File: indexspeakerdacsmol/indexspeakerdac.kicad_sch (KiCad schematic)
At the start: 34 parts, among them IC1 MAX98360AEFB+T, IC2 MAX98360AEFB+T, IC3 W25Q16JVUXIQ_TR, J1 Conn_01x04_Pin, J2 Conn_01x04_Pin, U1 RP2040, U2 MIC5317-3.3xM5, Y1 Crystal_GND24

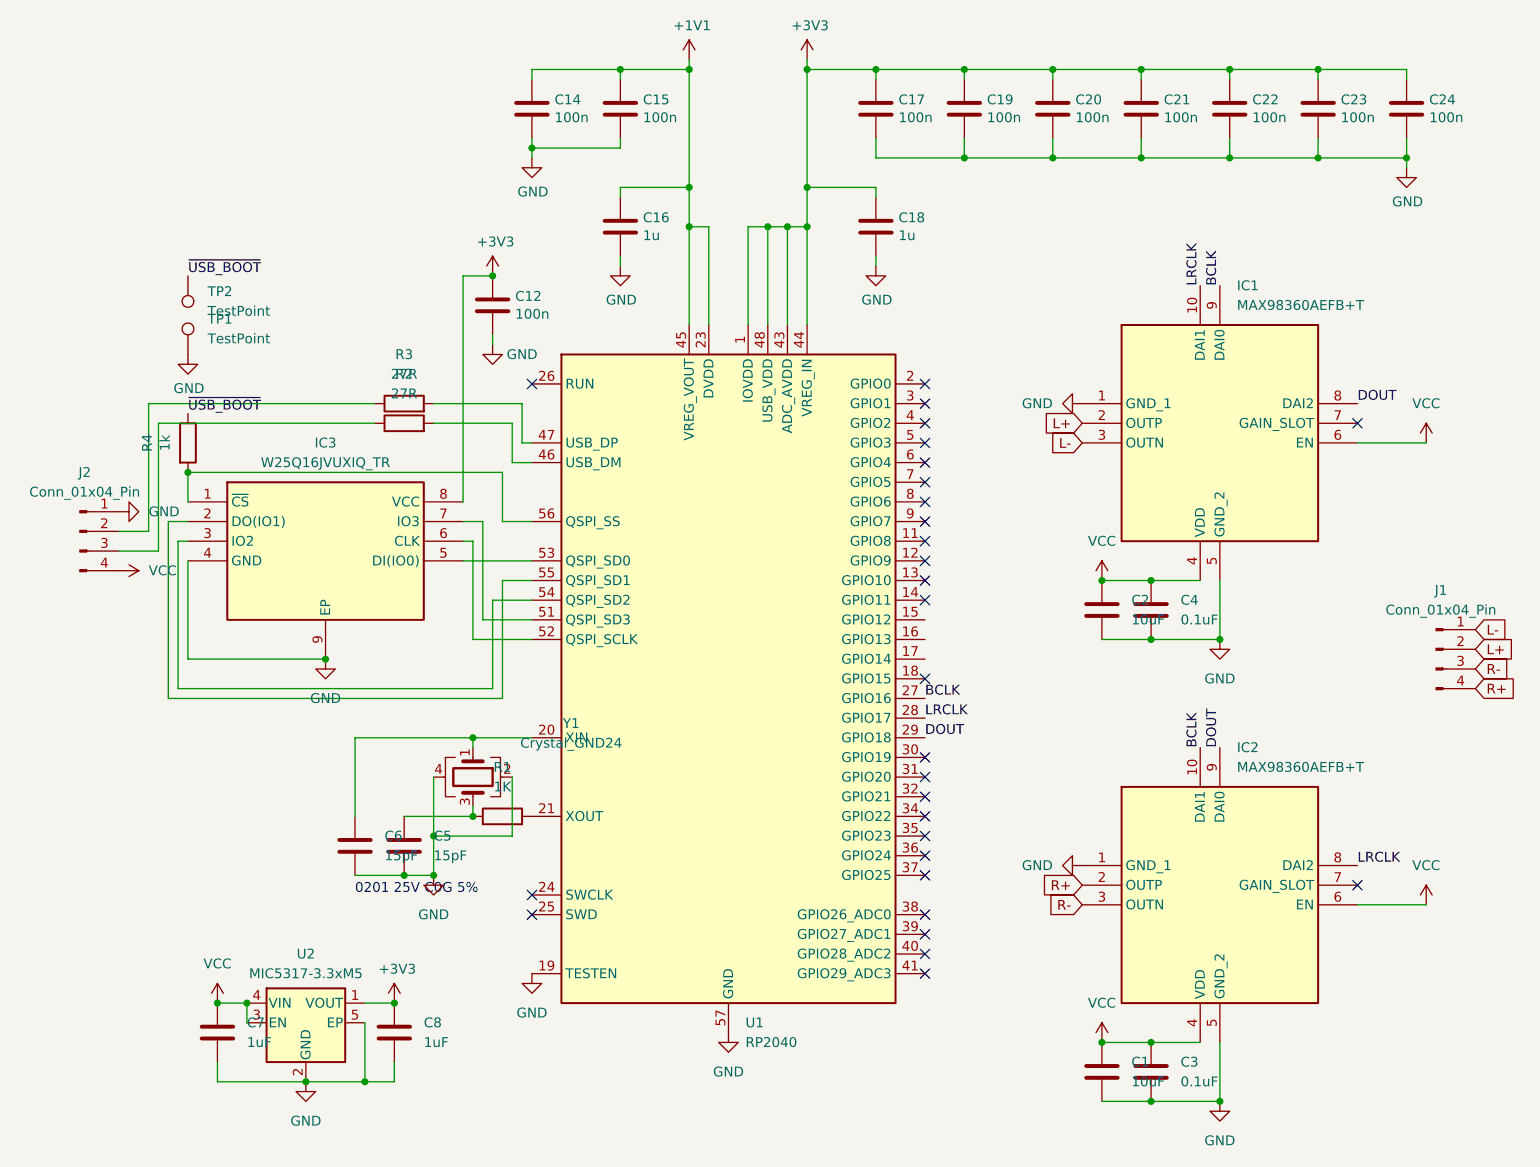
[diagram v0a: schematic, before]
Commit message: add bom
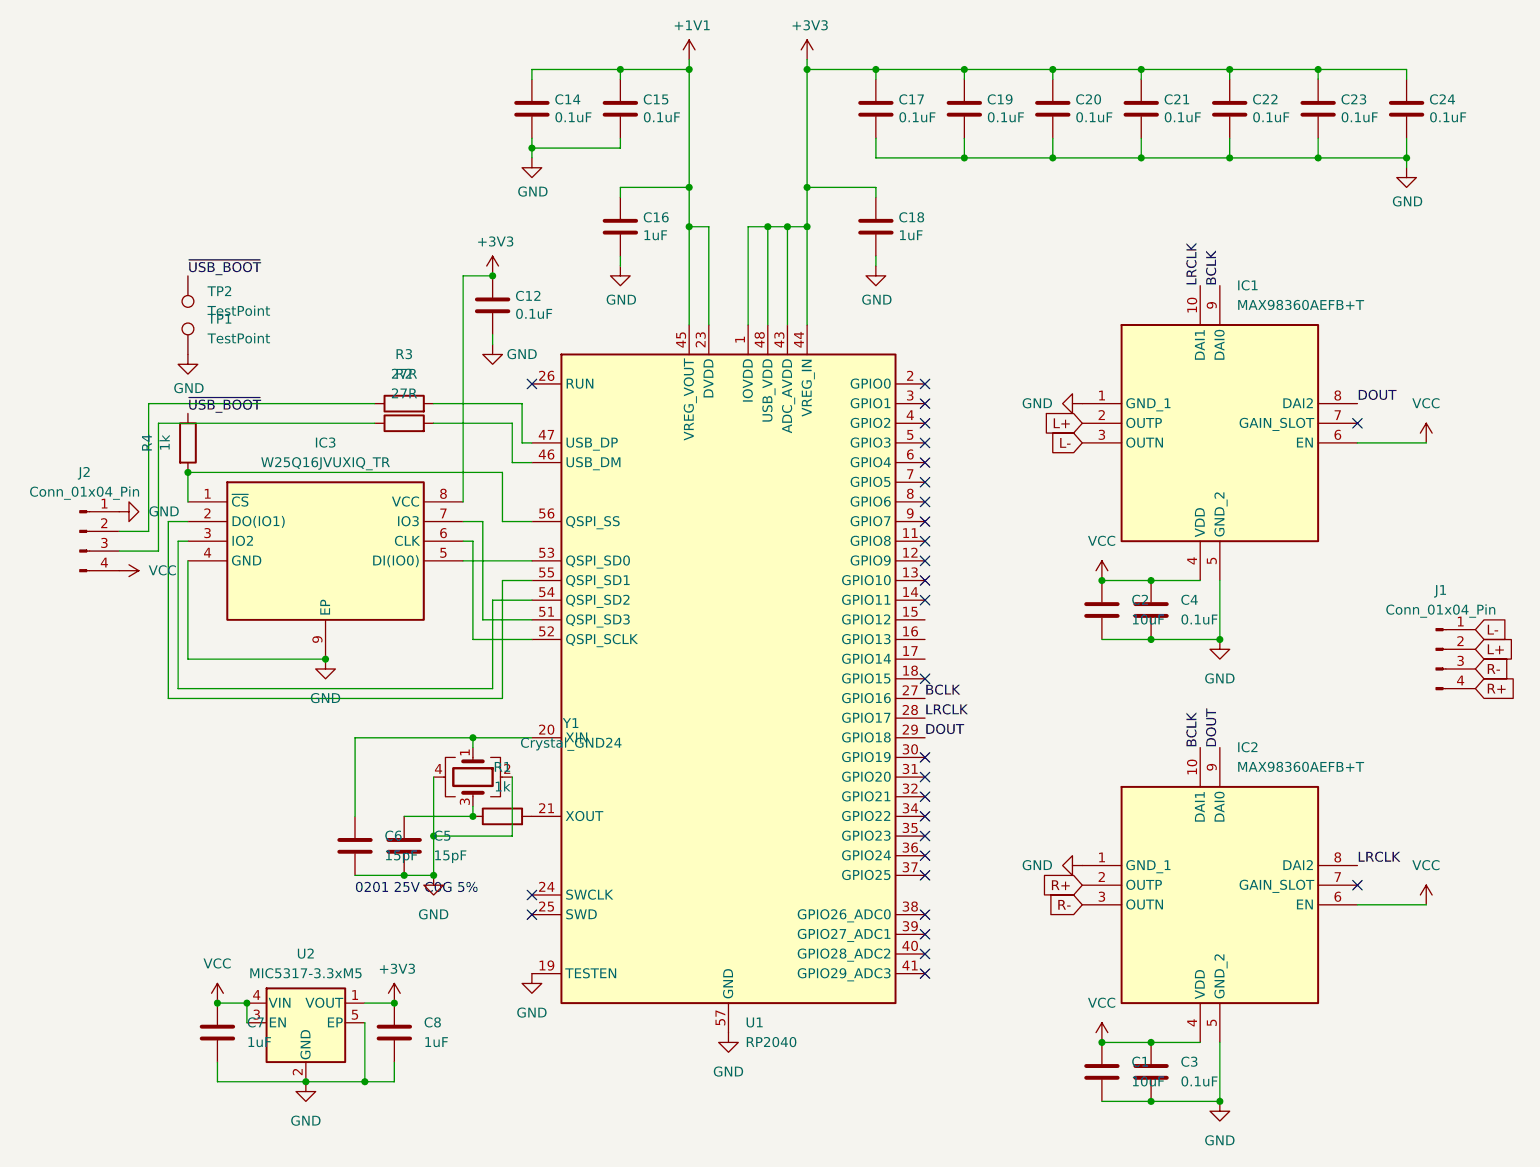
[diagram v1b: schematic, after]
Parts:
- C1, C2: Manufacturer_Name (none) -> Murata; Manufacturer_Part_Number (none) -> GRM188C81A106MA73D; Mouser Part Number (none) -> 81-GRM188C81A106MA3D
- C12, C14, C15, C17, C19, C20, C21, C22, C23, C24: value 100n -> 0.1uF; Manufacturer_Name (none) -> Murata; Manufacturer_Part_Number (none) -> GRM033C80J104KE15D; Mouser Part Number (none) -> 81-GRM33C80J104KE15D
- C16, C18: value 1u -> 1uF; Manufacturer_Name (none) -> Murata; Manufacturer_Part_Number (none) -> GRM155C81A105KA12J; Mouser Part Number (none) -> 81-GRM155C81A105KA2J
- C3, C4: Manufacturer_Name (none) -> Murata; Manufacturer_Part_Number (none) -> GRM155R61A104KA01J; Mouser Part Number (none) -> 81-GRM15R61A104KA01J
- C5, C6: Manufacturer_Name (none) -> Murata; Manufacturer_Part_Number (none) -> GRM0335C1E150JA01D; Mouser Part Number (none) -> 81-GRM0335C1E150JA1D
- C7, C8: Manufacturer_Name (none) -> Murata; Manufacturer_Part_Number (none) -> GRM155C81A105KA12J; Mouser Part Number (none) -> 81-GRM155C81A105KA2J
- IC1, IC2: Manufacturer_Name Analog Devices -> Analog Devices Inc.; Mouser Price/Stock https://www.mouser.co.uk/ProductDetail/Maxim-Integrated/MAX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 -> (none)
- IC3: Height 0.6 -> (none); Mouser Price/Stock https://www.mouser.co.uk/ProductDetail/Winbond/W25Q16JVUXIQ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 -> (none)
- R1: value 1K -> 1k; Manufacturer_Name (none) -> Vishay; Manufacturer_Part_Number (none) -> CRCW04021K00FKED; Mouser Part Number (none) -> 71-CRCW0402-1.0K-E3
- R2, R3: Manufacturer_Name (none) -> YAGEO; Manufacturer_Part_Number (none) -> RC0201FR-0727RL; Mouser Part Number (none) -> 603-RC0201FR-0727RL
- R4: Manufacturer_Name (none) -> Bourns; Manufacturer_Part_Number (none) -> CR0201-FW-1001GLF; Mouser Part Number (none) -> 652-CR0201FW-1001GLF
- U1: Manufacturer_Name (none) -> Raspberry Pi; Manufacturer_Part_Number (none) -> SC0914(7); Mouser Part Number (none) -> 358-SC09147
- U2: Manufacturer_Name (none) -> Microchip; Manufacturer_Part_Number (none) -> MIC5317-3.3YMT-TR; Mouser Part Number (none) -> 494-MIC531733YMTTR
- Y1: Manufacturer_Name (none) -> ECS; Manufacturer_Part_Number (none) -> ECS-120-10-33-AGM-TR; Mouser Part Number (none) -> 520-120-10-33-AGMT
